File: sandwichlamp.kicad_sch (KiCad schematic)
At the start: 17 parts, among them J1 Pole1, J2 Pole2, J3 Pole3, J4 12V Enable, J5 HLK-LD2410C, SW1 Rader Power, SW2 Power, U1 magnetic-charger, U3 hw357, U4 RX480E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

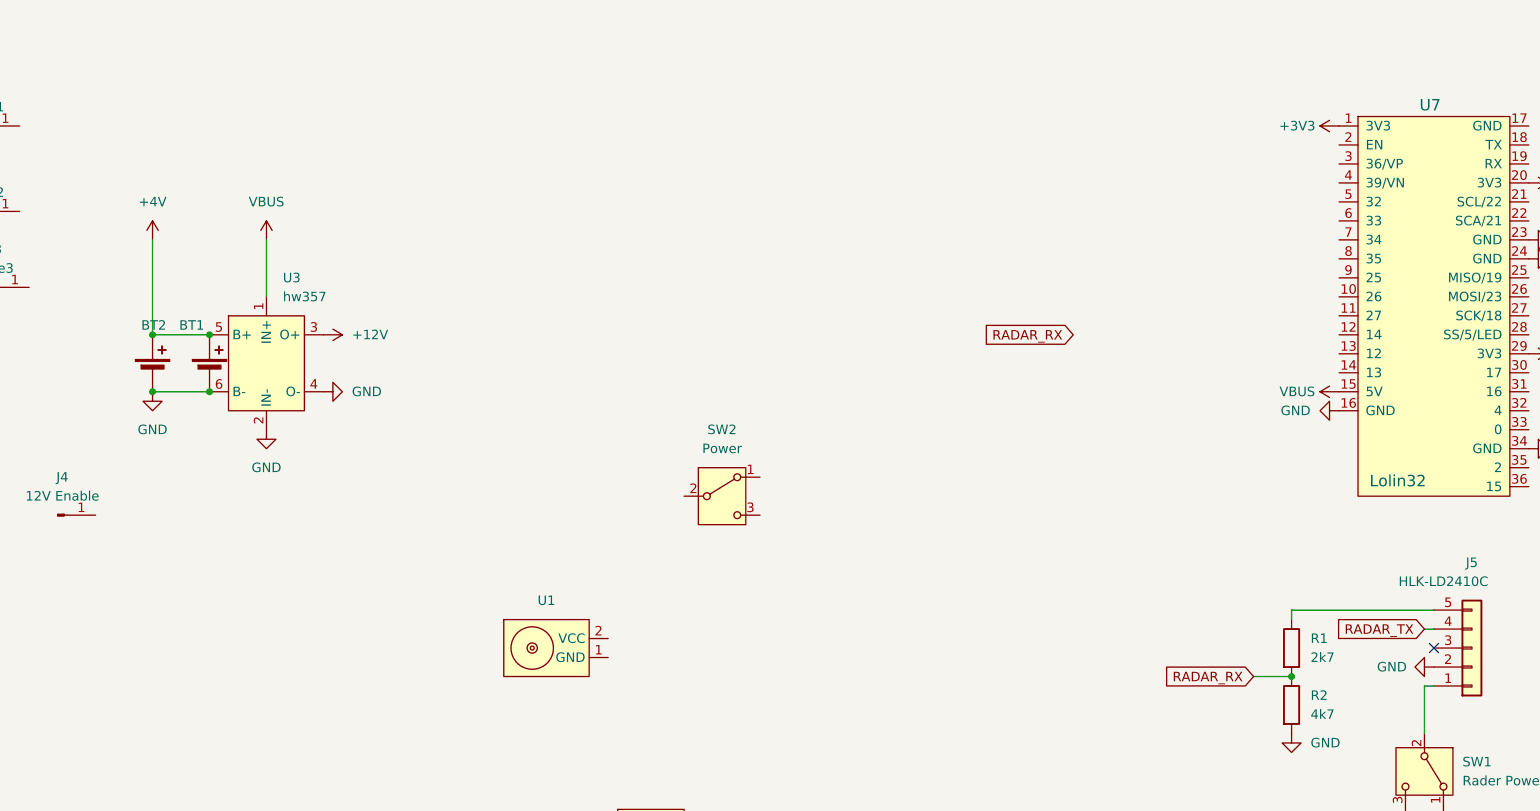
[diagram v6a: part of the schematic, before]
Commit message: Add battery pad to the Lolin where the battery voltage can be taken for the ESP
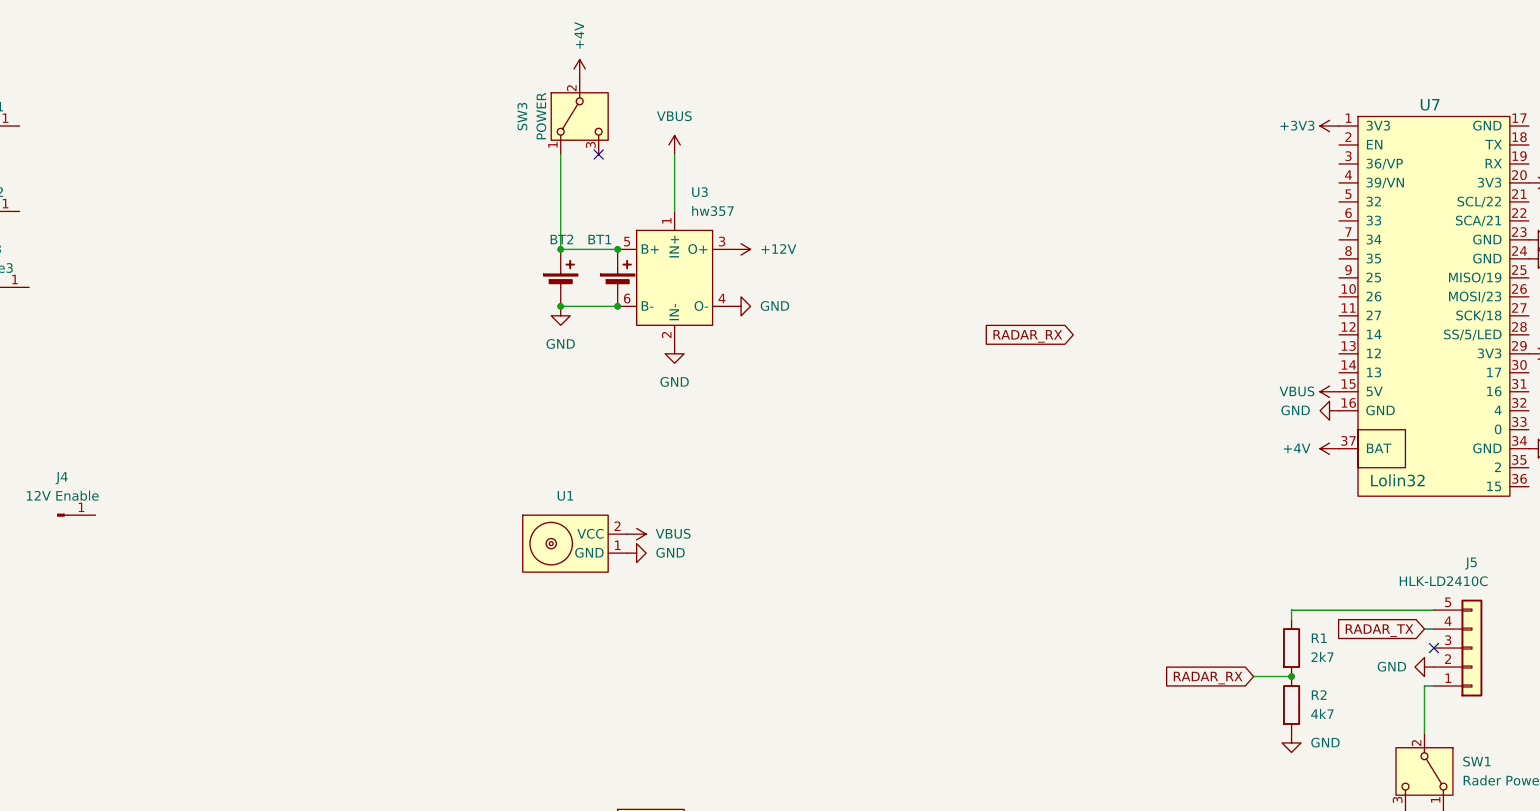
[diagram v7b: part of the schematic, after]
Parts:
- removed SW2: Power, Connector_PinHeader_2.54mm:PinHeader_1x03_P2.54mm_Vertical, symbol Switch:SW_SPDT
- added SW3: POWER, as12ap:as12ap, symbol Switch:SW_SPDT
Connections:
- net +4V: now also U7.37 (BAT), SW3.2 (B); no longer BT1.1 (+), BT2.1 (+), U3.5 (B+)
- net GND: now also U1.1 (GND)
- net VBUS: now also U1.2 (VCC)
- new net: BT1.1 (+), BT2.1 (+), SW3.1 (A), U3.5 (B+)
- no-connect marks 1 -> 2
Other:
- moved on the sheet: BT1, BT2, U1, U3

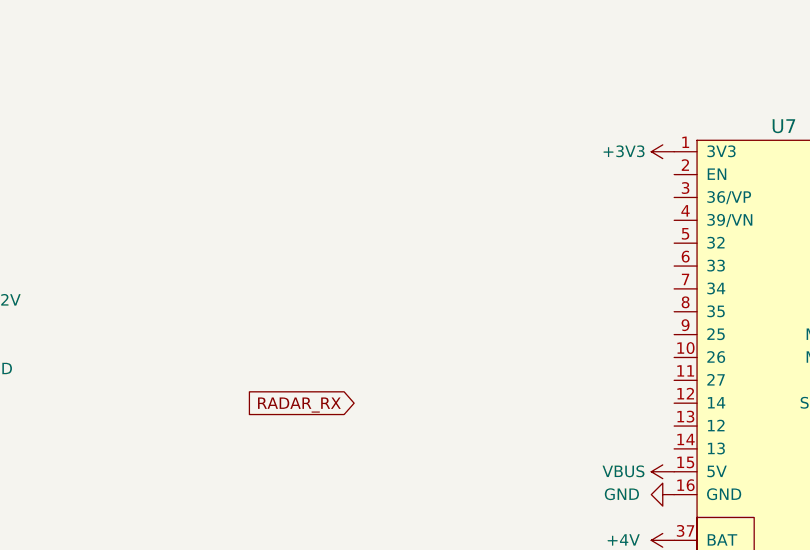
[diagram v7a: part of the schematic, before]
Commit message: Add M3 mounting holes
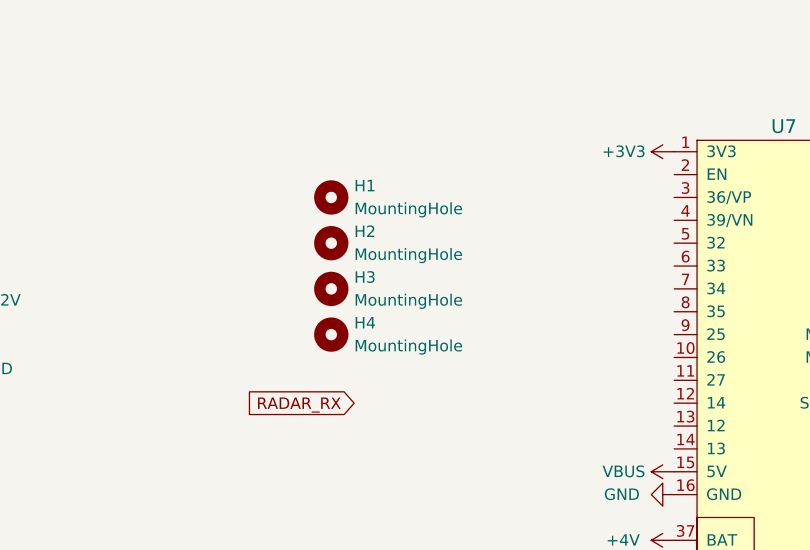
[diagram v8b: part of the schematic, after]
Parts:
- added H1, H2, H3, H4: MountingHole, MountingHole:MountingHole_3.2mm_M3, symbol Mechanical:MountingHole
- J2, J3: footprint MountingHole:MountingHole_6.4mm_M6_DIN965_Pad -> MountingHole:MountingHole_4.3mm_M4_ISO7380_Pad_TopOnly
